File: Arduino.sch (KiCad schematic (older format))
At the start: 0 parts

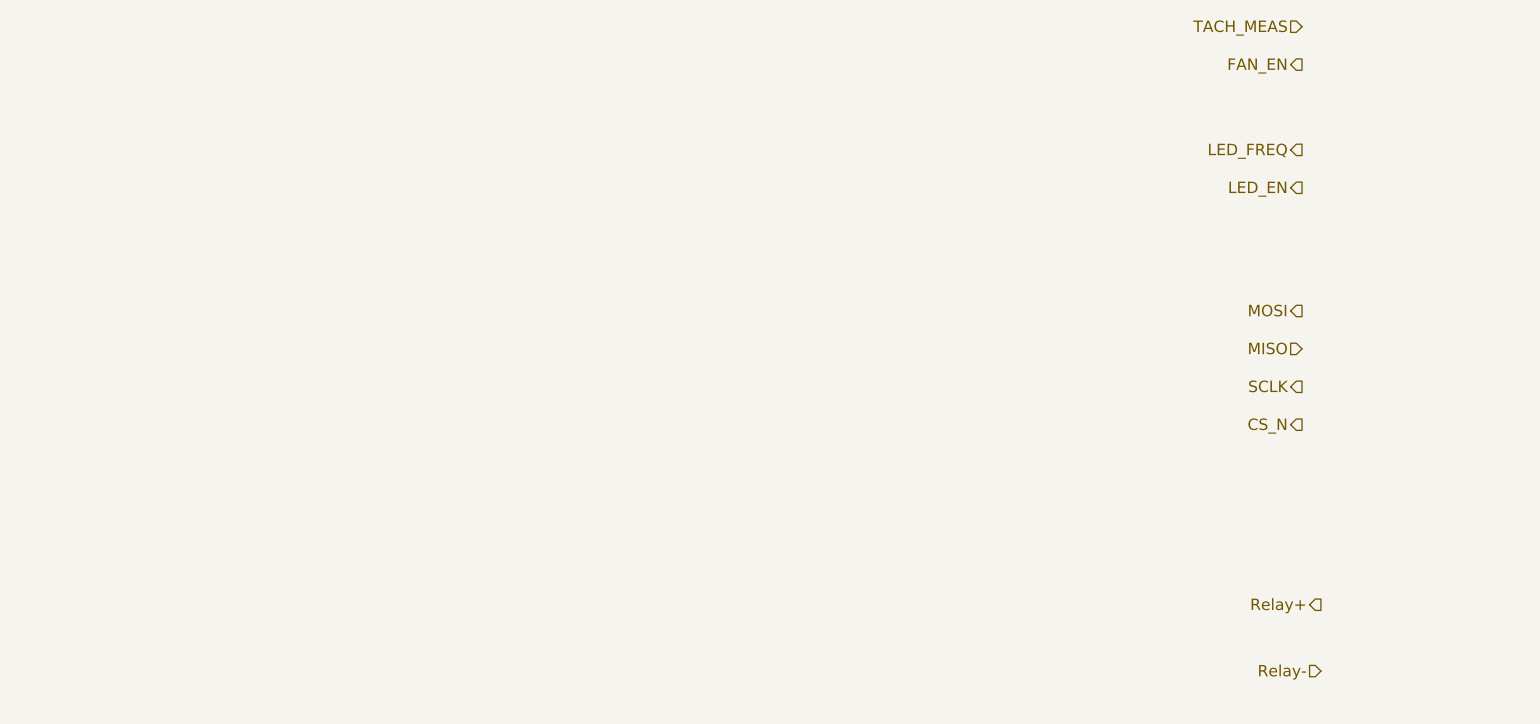
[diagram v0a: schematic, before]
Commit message: Changes up to and including Arduino module
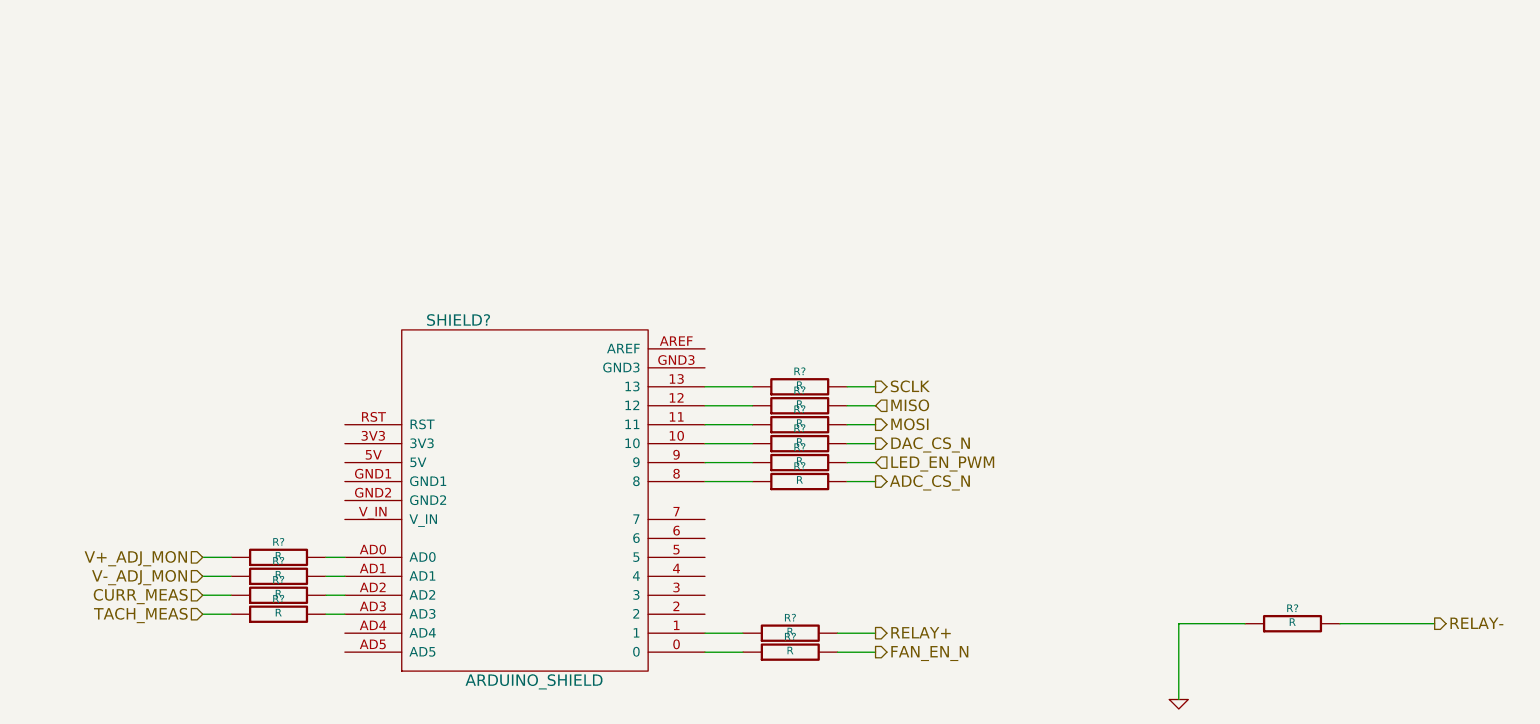
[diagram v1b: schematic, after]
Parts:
- added R? (x13): R, ~, symbol R
- added SHIELD?: ARDUINO_SHIELD, symbol ARDUINO_SHIELD
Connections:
- net MISO: now also R?.2
- net MOSI: now also R?.2
- net SCLK: now also R?.2
- net TACH_MEAS: now also R?.1
- new net: R?.1, SHIELD?.0
- new net: R?.1, SHIELD?.1
- new net: R?.1, SHIELD?.10
- new net: R?.1, SHIELD?.11
- new net: R?.1, SHIELD?.12
- new net: R?.1, SHIELD?.13
- new net: R?.1, SHIELD?.8
- new net: R?.1, SHIELD?.9
- new net: R?.2, SHIELD?.AD0
- new net: R?.2, SHIELD?.AD1
- new net: R?.2, SHIELD?.AD2
- new net: R?.2, SHIELD?.AD3
- new net ADC_CS_N: R?.2
- new net CURR_MEAS: R?.1
- new net DAC_CS_N: R?.2
- new net FAN_EN_N: R?.2
- new net GND: R?.1
- new net LED_EN_PWM: R?.2
- new net RELAY+: R?.2
- new net RELAY-: R?.2
- new net V+_ADJ_MON: R?.1
- new net V-_ADJ_MON: R?.1

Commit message: Current/Fan updates
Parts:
- added R? (x2): R, ~, symbol R
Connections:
- net at SHIELD?.0: now also R?.1; no longer R?.1
- net at SHIELD?.10: now also R?.1; no longer R?.1
- net at SHIELD?.7: now also R?.1
- net at SHIELD?.V_IN: now also R?.2
- net FAN_EN_N renamed FAN_PWM
- new net FAN_MODE: R?.2
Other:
- moved on the sheet: R?
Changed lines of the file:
@@
 $Descr A4 11693 8268
 encoding utf-8
-Sheet 2 9
+Sheet 9 9
 Title ""
-Date "12 feb 2014"
+Date "13 feb 2014"
 Rev ""
 Comp ""
@@
 Text HLabel 5500 4650 2    60   Output ~ 0
 RELAY+
-Text HLabel 8450 4600 2    60   Output ~ 0
-RELAY-
 Text HLabel 5500 3550 2    60   Output ~ 0
 MOSI
@@
 Text HLabel 5500 3350 2    60   Output ~ 0
 SCLK
+Text HLabel 5500 4050 2    60   Output ~ 0
+DAC_CS_N
 Text HLabel 5500 3650 2    60   Output ~ 0
-DAC_CS_N
-Text HLabel 5500 4750 2    60   Output ~ 0
-FAN_EN_N
-Text HLabel 1950 4550 0    60   Input ~ 0
+FAN_PWM
+Text HLabel 1700 4550 0    60   Input ~ 0
 TACH_MEAS
 $Comp
@@
 	1    0    0    -1
 $EndComp
-Text HLabel 1950 4450 0    60   Input ~ 0
+Text HLabel 1700 4450 0    60   Input ~ 0
 CURR_MEAS
 $Comp
 L R R?
 U 1 1 52F9AA9A
-P 5050 4750
-F 0 "R?" V 5130 4750 40  0000 C CNN
-F 1 "R" V 5057 4751 40  0000 C CNN
-F 2 "~" V 4980 4750 30  0000 C CNN
-F 3 "~" H 5050 4750 30  0000 C CNN
-	1    5050 4750
-	0    -1   -1   0
-$EndComp
-Wire Wire Line
-	4600 4750 4800 4750
-Wire Wire Line
-	5300 4750 5500 4750
+P 5100 3650
+F 0 "R?" V 5180 3650 40  0000 C CNN
+F 1 "R" V 5107 3651 40  0000 C CNN
+F 2 "~" V 5030 3650 30  0000 C CNN
+F 3 "~" H 5100 3650 30  0000 C CNN
+	1    5100 3650
+	0    -1   -1   0
+$EndComp
+Wire Wire Line
+	4600 3650 4850 3650
+Wire Wire Line
+	5350 3650 5500 3650
 $Comp
 L R R?
@@
 L R R?
 U 1 1 52F9B1EB
-P 2350 4550
-F 0 "R?" V 2430 4550 40  0000 C CNN
-F 1 "R" V 2357 4551 40  0000 C CNN
-F 2 "~" V 2280 4550 30  0000 C CNN
-F 3 "~" H 2350 4550 30  0000 C CNN
-	1    2350 4550
+P 2200 4550
+F 0 "R?" V 2280 4550 40  0000 C CNN
+F 1 "R" V 2207 4551 40  0000 C CNN
+F 2 "~" V 2130 4550 30  0000 C CNN
+F 3 "~" H 2200 4550 30  0000 C CNN
+	1    2200 4550
 	0    -1   -1   0
 $EndComp
@@
 L R R?
 U 1 1 52F9B1F1
-P 2350 4450
-F 0 "R?" V 2430 4450 40  0000 C CNN
-F 1 "R" V 2357 4451 40  0000 C CNN
-F 2 "~" V 2280 4450 30  0000 C CNN
-F 3 "~" H 2350 4450 30  0000 C CNN
-	1    2350 4450
-	0    -1   -1   0
-$EndComp
-Wire Wire Line
-	2100 4450 1950 4450
-Wire Wire Line
-	1950 4550 2100 4550
-Wire Wire Line
-	2600 4550 2700 4550
-Wire Wire Line
-	2700 4450 2600 4450
-Text HLabel 1950 4250 0    60   Input ~ 0
+P 2200 4450
+F 0 "R?" V 2280 4450 40  0000 C CNN
+F 1 "R" V 2207 4451 40  0000 C CNN
+F 2 "~" V 2130 4450 30  0000 C CNN
+F 3 "~" H 2200 4450 30  0000 C CNN
+	1    2200 4450
+	0    -1   -1   0
+$EndComp
+Wire Wire Line
+	1950 4450 1700 4450
+Wire Wire Line
+	1700 4550 1950 4550
+Wire Wire Line
+	2450 4550 2700 4550
+Wire Wire Line
+	2450 4450 2700 4450
+Text HLabel 1700 4250 0    60   Input ~ 0
 V+_ADJ_MON
-Text HLabel 1950 4350 0    60   Input ~ 0
+Text HLabel 1700 4350 0    60   Input ~ 0
 V-_ADJ_MON
 $Comp
 L R R?
 U 1 1 52F9B78B
-P 2350 4350
-F 0 "R?" V 2430 4350 40  0000 C CNN
-F 1 "R" V 2357 4351 40  0000 C CNN
-F 2 "~" V 2280 4350 30  0000 C CNN
-F 3 "~" H 2350 4350 30  0000 C CNN
-	1    2350 4350
+P 2200 4350
+F 0 "R?" V 2280 4350 40  0000 C CNN
+F 1 "R" V 2207 4351 40  0000 C CNN
+F 2 "~" V 2130 4350 30  0000 C CNN
+F 3 "~" H 2200 4350 30  0000 C CNN
+	1    2200 4350
 	0    -1   -1   0
 $EndComp
@@
 L R R?
 U 1 1 52F9B791
-P 2350 4250
-F 0 "R?" V 2430 4250 40  0000 C CNN
-F 1 "R" V 2357 4251 40  0000 C CNN
-F 2 "~" V 2280 4250 30  0000 C CNN
-F 3 "~" H 2350 4250 30  0000 C CNN
-	1    2350 4250
-	0    -1   -1   0
-$EndComp
-Wire Wire Line
-	2600 4250 2700 4250
-Wire Wire Line
-	2700 4350 2600 4350
-Wire Wire Line
-	1950 4250 2100 4250
-Wire Wire Line
-	1950 4350 2100 4350
+P 2200 4250
+F 0 "R?" V 2280 4250 40  0000 C CNN
+F 1 "R" V 2207 4251 40  0000 C CNN
+F 2 "~" V 2130 4250 30  0000 C CNN
+F 3 "~" H 2200 4250 30  0000 C CNN
+	1    2200 4250
+	0    -1   -1   0
+$EndComp
+Wire Wire Line
+	2450 4250 2700 4250
+Wire Wire Line
+	2450 4350 2700 4350
+Wire Wire Line
+	1700 4250 1950 4250
+Wire Wire Line
+	1700 4350 1950 4350
 $Comp
 L R R?
@@
 L R R?
 U 1 1 52F9BF24
-P 5100 3650
-F 0 "R?" V 5180 3650 40  0000 C CNN
-F 1 "R" V 5107 3651 40  0000 C CNN
-F 2 "~" V 5030 3650 30  0000 C CNN
-F 3 "~" H 5100 3650 30  0000 C CNN
-	1    5100 3650
-	0    -1   -1   0
-$EndComp
-Wire Wire Line
-	4600 3650 4850 3650
+P 5100 4050
+F 0 "R?" V 5180 4050 40  0000 C CNN
+F 1 "R" V 5107 4051 40  0000 C CNN
+F 2 "~" V 5030 4050 30  0000 C CNN
+F 3 "~" H 5100 4050 30  0000 C CNN
+	1    5100 4050
+	0    -1   -1   0
+$EndComp
+Wire Wire Line
+	4600 4050 4850 4050
 Wire Wire Line
 	4600 3750 4850 3750
@@
 	5350 3750 5500 3750
 Wire Wire Line
-	5350 3650 5500 3650
+	5350 4050 5500 4050
 $Comp
 L R R?
@@
 Wire Wire Line
 	5350 3850 5500 3850
+Text HLabel 5500 4750 2    60   Input ~ 0
+FAN_MODE
+$Comp
+L R R?
+U 1 1 52FC5FD5
+P 5050 4750
+F 0 "R?" V 5130 4750 40  0000 C CNN
+F 1 "R" V 5057 4751 40  0000 C CNN
+F 2 "~" V 4980 4750 30  0000 C CNN
+F 3 "~" H 5050 4750 30  0000 C CNN
+	1    5050 4750
+	0    -1   -1   0
+$EndComp
+Wire Wire Line
+	5300 4750 5500 4750
+Wire Wire Line
+	4800 4750 4600 4750
+$Comp
+L R R?
+U 1 1 52FC6266
+P 2200 4050
+F 0 "R?" V 2280 4050 40  0000 C CNN
+F 1 "R" V 2207 4051 40  0000 C CNN
+F 2 "~" V 2130 4050 30  0000 C CNN
+F 3 "~" H 2200 4050 30  0000 C CNN
+	1    2200 4050
+	0    -1   -1   0
+$EndComp
+Wire Wire Line
+	2450 4050 2700 4050
+$Comp
+L +12P #PWR?
+U 1 1 52FC630E
+P 1400 3700
+F 0 "#PWR?" H 1400 3670 30  0001 C CNN
+F 1 "+12P" H 1400 3800 30  0000 C CNN
+F 2 "" H 1400 3700 60  0000 C CNN
+F 3 "" H 1400 3700 60  0000 C CNN
+	1    1400 3700
+	1    0    0    -1
+$EndComp
+Wire Wire Line
+	1400 3750 1400 4050
+Wire Wire Line
+	1400 4050 1950 4050
+Text HLabel 8450 4600 2    60   Input ~ 0
+RELAY-
 $EndSCHEMATC
